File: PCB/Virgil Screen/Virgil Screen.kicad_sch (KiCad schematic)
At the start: 13 parts, among them J3 SFV20R-2STE1HLF, Q1 SS8550, U1 XIAO-RP2350-SMD, U2 ZJY114TC-IF03-HSD, U4 SN74LVC1T45DBV

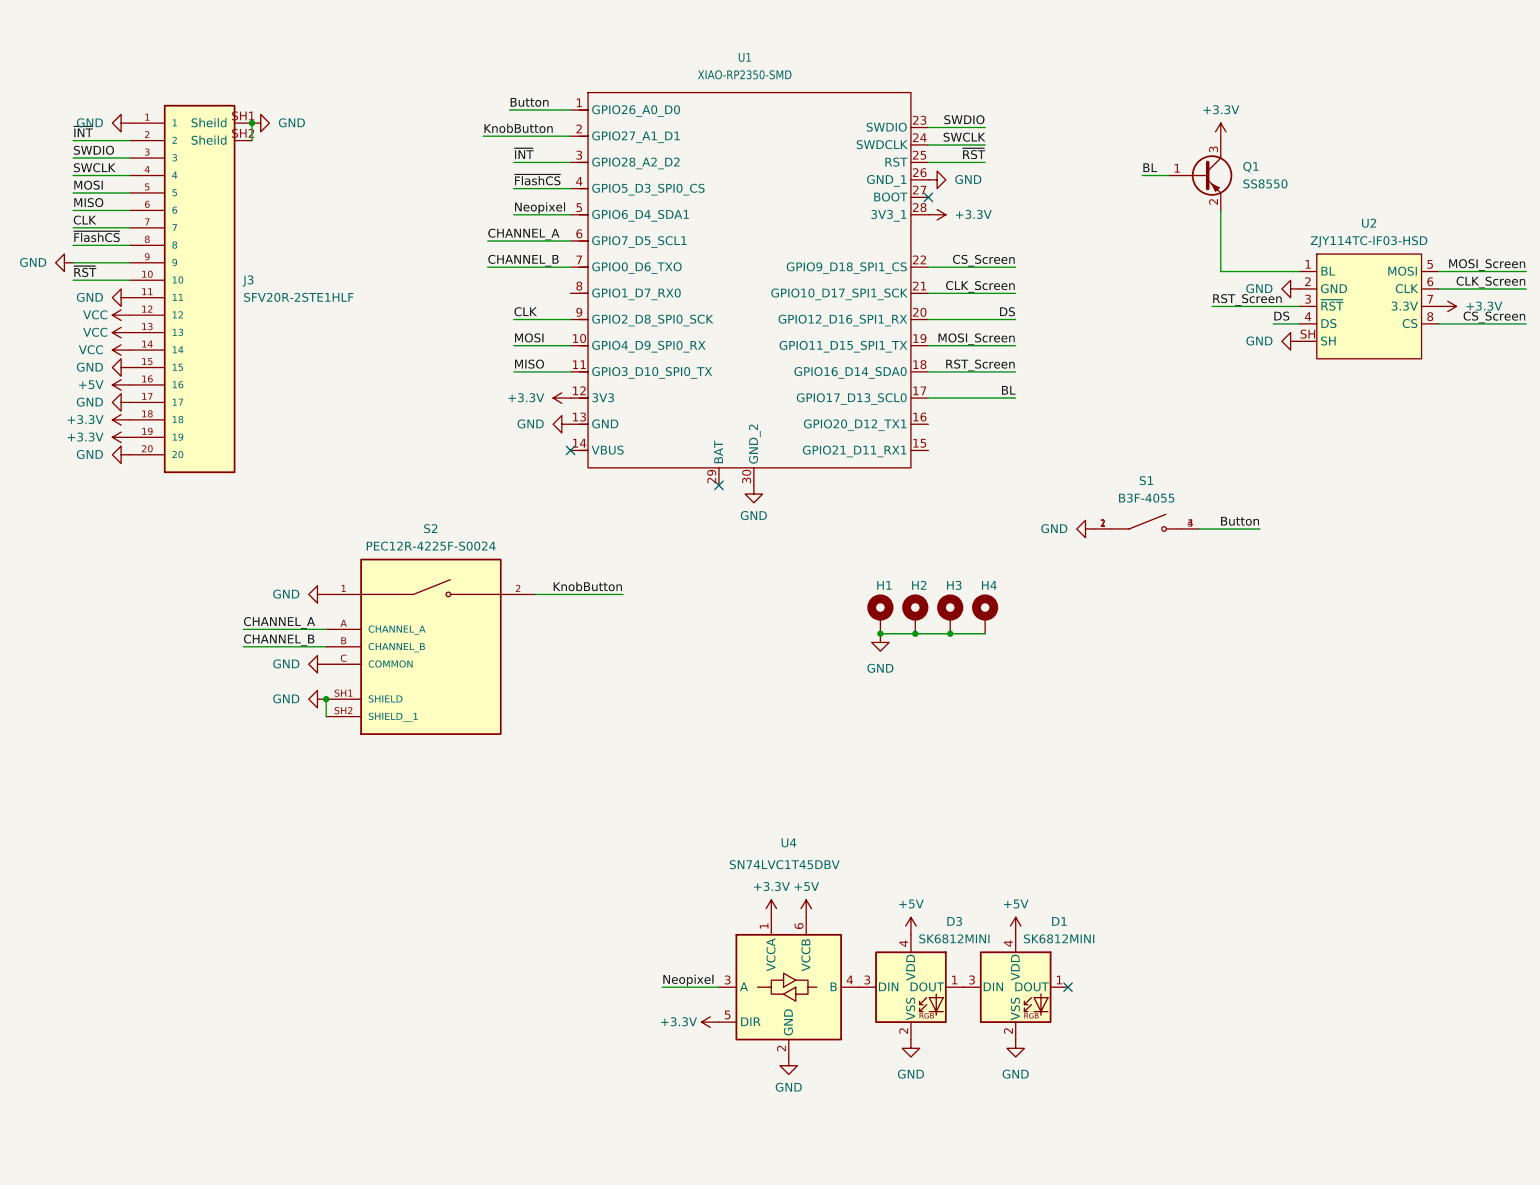
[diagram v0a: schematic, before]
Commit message: Updated PCBs to use raw rp2040s
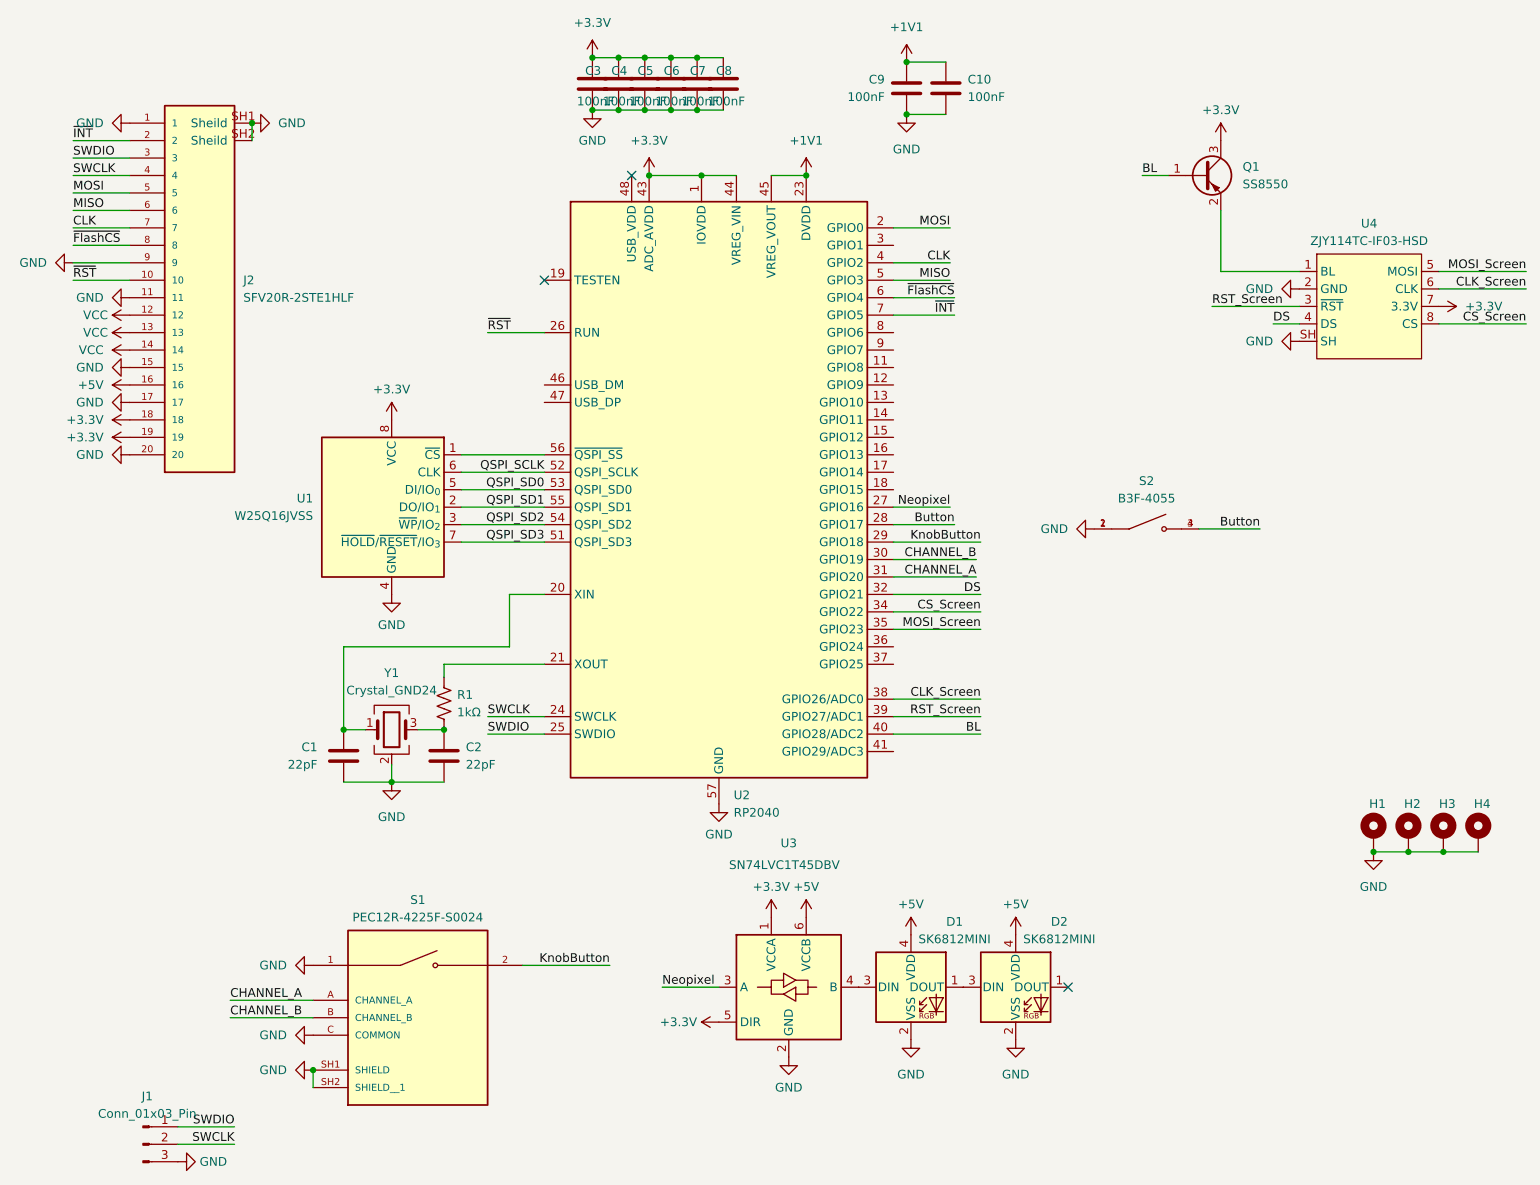
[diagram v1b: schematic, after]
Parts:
- removed U1: XIAO-RP2350-SMD, Snapeda:XIAO-RP2350-SMD, symbol Snapeda:XIAO-RP2350-SMD
- added C1, C2: 22pF, Capacitor_SMD:C_0603_1608Metric, symbol Device:C
- added C10, C3, C4, C5, C6, C7, C8, C9: 100nF, Capacitor_SMD:C_0603_1608Metric, symbol Device:C
- added J1: Conn_01x03_Pin, Connector_PinHeader_2.54mm:PinHeader_1x03_P2.54mm_Vertical, symbol Connector:Conn_01x03_Pin
- added R1: 1kΩ, Resistor_SMD:R_0603_1608Metric, symbol Device:R_US
- added U1: W25Q16JVSS, Package_SO:SOIC-8_5.3x5.3mm_P1.27mm, symbol Memory_Flash:W25Q16JVSS
- added U2: RP2040, Package_DFN_QFN:QFN-56-1EP_7x7mm_P0.4mm_EP3.2x3.2mm, symbol MCU_RaspberryPi:RP2040
- added Y1: Crystal_GND24, Crystal:Crystal_SMD_Abracon_ABM8G-4Pin_3.2x2.5mm, symbol Device:Crystal_GND24
- renumbered D3 to D1, D1 to D2, J3 to J2, S2 to S1, S1 to S2, U4 to U3, U2 to U4
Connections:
- net +3.3V: now also C3.1, C4.1, C5.1, C6.1, C7.1, C8.1, U1.8 (VCC), U2.1 (IOVDD), U2.10 (IOVDD), U2.22 (IOVDD), U2.33 (IOVDD), U2.42 (IOVDD), U2.43 (ADC_AVDD), U2.44 (VREG_VIN), U2.49 (IOVDD)
- net BL: now also U2.40 (GPIO28/ADC2)
- net Button: now also U2.28 (GPIO17)
- net CHANNEL_A: now also U2.31 (GPIO20)
- net CHANNEL_B: now also U2.30 (GPIO19)
- net CLK: now also U2.4 (GPIO2)
- net CLK_Screen: now also U2.38 (GPIO26/ADC0)
- net CS_Screen: now also U2.34 (GPIO22)
- net DS: now also U2.32 (GPIO21)
- net GND: now also C1.1, C10.2, C2.1, C3.2, C4.2, C5.2, C6.2, C7.2, C8.2, C9.2, J1.3 (Pin_3), U1.4 (GND), U2.57 (GND), Y1.2 (G), Y1.4 (G)
- net KnobButton: now also U2.29 (GPIO18)
- net MISO: now also U2.5 (GPIO3)
- net MOSI: now also U2.2 (GPIO0)
- net MOSI_Screen: now also U2.35 (GPIO23)
- net Neopixel: now also U2.27 (GPIO16)
- net RST_Screen: now also U2.39 (GPIO27/ADC1)
- net SWCLK: now also J1.2 (Pin_2), U2.24 (SWCLK)
- net SWDIO: now also J1.1 (Pin_1), U2.25 (SWDIO)
- net ~{FlashCS}: now also U2.6 (GPIO4)
- net ~{INT}: now also U2.7 (GPIO5)
- net ~{RST}: now also U2.26 (RUN)
- new net: R1.1, U2.21 (XOUT)
- new net: C2.2, R1.2, Y1.3
- new net: C1.2, U2.20 (XIN), Y1.1
- new net: U1.1 (~{CS}), U2.56 (~{QSPI_SS})
- new net +1V1: C10.1, C9.1, U2.23 (DVDD), U2.45 (VREG_VOUT), U2.50 (DVDD)
- new net QSPI_SCLK: U1.6 (CLK), U2.52 (QSPI_SCLK)
- new net QSPI_SD0: U1.5 (DI/IO_{0}), U2.53 (QSPI_SD0)
- new net QSPI_SD1: U1.2 (DO/IO_{1}), U2.55 (QSPI_SD1)
- new net QSPI_SD2: U1.3 (~{WP}/IO_{2}), U2.54 (QSPI_SD2)
- new net QSPI_SD3: U1.7 (~{HOLD}/~{RESET}/IO_{3}), U2.51 (QSPI_SD3)
- no-connect marks 4 -> 3
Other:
- moved on the sheet: H1, H2, H3, H4, S1

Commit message: Finished PCBs
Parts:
- removed C3: 100nF, Capacitor_SMD:C_0603_1608Metric, symbol Device:C
- removed J1: Conn_01x03_Pin, Connector_PinHeader_2.54mm:PinHeader_1x03_P2.54mm_Vertical, symbol Connector:Conn_01x03_Pin
- C1, C2: value 22pF -> 15pF
- J2: value SFV20R-2STE1HLF -> AFC07-S20FCC-00
- U4: value ZJY114TC-IF03-HSD -> AFC07-S08ECC-00
- Y1: value Crystal_GND24 -> ABM8-272-T3

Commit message: Started code, commiting before adding submodules
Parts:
- J2: footprint Snapeda:AMPHENOL_SFV20R-2STE1HLF -> Snapeda:JUSHUO AFC07-S20FCC-00
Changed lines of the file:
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@@
 			)
 		)
-		(property "Footprint" "Snapeda:AMPHENOL_SFV20R-2STE1HLF"
+		(property "Footprint" "Snapeda:JUSHUO AFC07-S20FCC-00"
 			(at 46.355 52.705 0)
 			(hide yes)
